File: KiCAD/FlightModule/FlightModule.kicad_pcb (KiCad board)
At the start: 2 copper layers, 90 x 70 mm, 19 parts, among them Q1 AO3400A, Q2 AO3400A, U1 ARDUINO_MKR_WAN_1310, U2 MCP2515-xST, U3 MCP2562-E-SN, U4 MB85RQ8MX, U5 MB85RQ8MX, U6 MB85RQ8MX

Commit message: 配線8割り終わり．次の作業....
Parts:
- removed IC1: ~, GPSShield:UBLOXLIB_SAM-M8Q
- removed U4, U6: MB85RQ8MX, Package_SO:SOIC-16W_7.5x10.3mm_P1.27mm
- added C10: 1u, Capacitor_SMD:C_0603_1608Metric_Pad1.08x0.95mm_HandSolder, F.Cu at (185.2, 104.9)
- added C11: 1u, Capacitor_SMD:C_0603_1608Metric_Pad1.08x0.95mm_HandSolder, F.Cu at (185.2, 98.6)
- added C13: 0.1uF, Capacitor_SMD:C_0603_1608Metric_Pad1.08x0.95mm_HandSolder, F.Cu at (160.5, 114.9)
- added C14: 0.1uF, Capacitor_SMD:C_0603_1608Metric_Pad1.08x0.95mm_HandSolder, B.Cu at (154.2, 105.5)
- added C15: 0.1uF, Capacitor_SMD:C_0603_1608Metric_Pad1.08x0.95mm_HandSolder, B.Cu at (122.7, 94.5)
- added C16: 1uF, Capacitor_SMD:C_1206_3216Metric_Pad1.33x1.80mm_HandSolder, F.Cu at (153.7, 68.1)
- added C17: 1uF, Capacitor_SMD:C_1206_3216Metric_Pad1.33x1.80mm_HandSolder, F.Cu at (166.1, 68.1)
- added C4: 0.1uF, Capacitor_SMD:C_0603_1608Metric_Pad1.08x0.95mm_HandSolder, F.Cu at (160.5, 120.1)
- added C5: 0.1uF, Capacitor_SMD:C_0603_1608Metric_Pad1.08x0.95mm_HandSolder, B.Cu at (170.9, 110.2)
- added C6: 15pF, Capacitor_SMD:C_0603_1608Metric_Pad1.08x0.95mm_HandSolder, B.Cu at (180.8, 94.1)
- added C7: 15pF, Capacitor_SMD:C_0603_1608Metric_Pad1.08x0.95mm_HandSolder, B.Cu at (164.3, 94.1)
- added C8: 0.1uF, Capacitor_SMD:C_0603_1608Metric_Pad1.08x0.95mm_HandSolder, B.Cu at (137.5, 120.8)
- added C9: 0.1uF, Capacitor_SMD:C_0603_1608Metric_Pad1.08x0.95mm_HandSolder, F.Cu at (135.6, 117.2)
- added D10: Green, LED_SMD:LED_0603_1608Metric_Pad1.05x0.95mm_HandSolder, F.Cu at (135.6, 67.0)
- added D11: GS1010FL, Diode_SMD:D_SOD-123F, F.Cu at (136.1, 75.4)
- added D12: Blue, LED_SMD:LED_0603_1608Metric_Pad1.05x0.95mm_HandSolder, F.Cu at (90.9, 82.5)
- added D7: Blue, LED_SMD:LED_0603_1608Metric_Pad1.05x0.95mm_HandSolder, F.Cu at (90.9, 80.0)
- added D8: Green, LED_SMD:LED_0603_1608Metric_Pad1.05x0.95mm_HandSolder, F.Cu at (144.1, 67.0)
- added D9: GS1010FL, Diode_SMD:D_SOD-123F, F.Cu at (142.1, 75.4)
- added J1: DF11B-8DP-2DS, TSRP_Connector_Hirose:DF11-8DP-2DS, F.Cu at (162.5, 128.0)
- added J4: DF51-2P-2DS, TSRP_Connector_Hirose:DF51-2P-2DS, F.Cu at (137.5, 134.8)
- added J5: DF51A-4P-2DSA, TSRP_Connector_Hirose:DF51A-4P-2DSA, F.Cu at (141.6, 68.4)
- added PS1: M78AR05-0.5, TSRP_IC:M78AR03305, F.Cu at (181.7, 113.9)
- added R11: 120R, Resistor_SMD:R_0603_1608Metric_Pad0.98x0.95mm_HandSolder, F.Cu at (164.6, 121.9)
- added R13: 680R, Resistor_SMD:R_0603_1608Metric_Pad0.98x0.95mm_HandSolder, F.Cu at (86.6, 84.7)
- added R14: 10kR, Resistor_SMD:R_0603_1608Metric_Pad0.98x0.95mm_HandSolder, B.Cu at (173.0, 110.2)
- added R15: 300, Resistor_SMD:R_0603_1608Metric_Pad0.98x0.95mm_HandSolder, F.Cu at (140.3, 82.9)
- added R16: 10k, Resistor_SMD:R_0603_1608Metric_Pad0.98x0.95mm_HandSolder, F.Cu at (140.3, 85.0)
- added R17: 2.4k, Resistor_SMD:R_0603_1608Metric_Pad0.98x0.95mm_HandSolder, F.Cu at (147.6, 67.0)
- added R18: 300, Resistor_SMD:R_0603_1608Metric_Pad0.98x0.95mm_HandSolder, F.Cu at (134.1, 82.9)
- added R19: 10k, Resistor_SMD:R_0603_1608Metric_Pad0.98x0.95mm_HandSolder, F.Cu at (134.1, 85.0)
- added R20: 2.4k, Resistor_SMD:R_0603_1608Metric_Pad0.98x0.95mm_HandSolder, F.Cu at (139.3, 67.0)
- added R21: 680R, Resistor_SMD:R_0603_1608Metric_Pad0.98x0.95mm_HandSolder, F.Cu at (86.6, 87.2)
- added R24: 10kR, Resistor_SMD:R_0603_1608Metric_Pad0.98x0.95mm_HandSolder, F.Cu at (135.6, 115.4)
- added R25: 10kR, Resistor_SMD:R_0603_1608Metric_Pad0.98x0.95mm_HandSolder, B.Cu at (139.4, 122.6)
- added R26: 4.7kR, Resistor_SMD:R_0603_1608Metric_Pad0.98x0.95mm_HandSolder, B.Cu at (136.5, 105.4)
- added R27: 100k, Resistor_SMD:R_0603_1608Metric_Pad0.98x0.95mm_HandSolder, F.Cu at (169.9, 85.1)
- added R28: 0, Resistor_SMD:R_0603_1608Metric_Pad0.98x0.95mm_HandSolder, F.Cu at (160.8, 67.6)
- added R29: 4.7k, Resistor_SMD:R_0603_1608Metric_Pad0.98x0.95mm_HandSolder, F.Cu at (148.1, 84.8)
- added R30: 4.7k, Resistor_SMD:R_0603_1608Metric_Pad0.98x0.95mm_HandSolder, F.Cu at (149.6, 79.5)
- added U7: TC7S14F, Package_TO_SOT_SMD:TSOT-23-5_HandSoldering, F.Cu at (134.7, 120.3)
- added U8: MCP2562-E-SN, Package_SO:SOIC-8_3.9x4.9mm_P1.27mm, F.Cu at (164.6, 117.1)
- added U9: MCP2515-xST, Package_SO:TSSOP-20_4.4x6.5mm_P0.65mm, B.Cu at (170.7, 103.3)
- added Ux1: ARDUINO_MKR_WAN_1310, TSRP_Arduino:BOARD_ARDUINO_MKR_WAN_1310, F.Cu at (143.0, 100.0)
- added Y1: 8MHz, Crystal:Crystal_SMD_HC49-SD, B.Cu at (172.6, 95.1)
- D1, D3: value G -> Blue
- D2: value GS1010FL -> Blue; footprint Diode_SMD:D_SOD-123F -> LED_SMD:LED_0603_1608Metric_Pad1.05x0.95mm_HandSolder
- D4: value GS1010FL -> R; footprint Diode_SMD:D_SOD-123F -> LED_SMD:LED_0603_1608Metric_Pad1.05x0.95mm_HandSolder
- R1: value 300R -> 4.7kR; moved to B.Cu
- R2: value 10kR -> 4.7kR; moved to B.Cu
- R3: value 2.4kR -> 680R
- R4: value 300R -> 680R
- R5: value 10kR -> 680R
- U1: value ARDUINO_MKR_WAN_1310 -> MB85RQ8MX; footprint ARDUINO_MKR_WAN_1310:BOARD_ARDUINO_MKR_WAN_1310 -> Package_SO:SOIC-16W_7.5x10.3mm_P1.27mm; moved to B.Cu
- U2: value MCP2515-xST -> MB85RQ8MX; footprint Package_SO:TSSOP-20_4.4x6.5mm_P0.65mm -> Package_SO:SOIC-16W_7.5x10.3mm_P1.27mm; moved to B.Cu
- U3: value MCP2562-E-SN -> SAM-M8Q-0-10; footprint Package_SO:SOIC-8_3.9x4.9mm_P1.27mm -> TSRP_IC:MODULE_SAM-M8Q-0-10
- U5: value MB85RQ8MX -> NCV8114BSN330T1G; footprint Package_SO:SOIC-16W_7.5x10.3mm_P1.27mm -> Package_TO_SOT_SMD:TSOT-23-5
- moved D3 140.2 mm to (90.9, 77.2)
- moved R3 130.6 mm to (86.6, 77.2)
- moved R5 130.6 mm to (86.6, 82.2)
- moved R4 130.6 mm to (86.6, 79.7)
- moved D1 122.6 mm to (90.9, 72.2)
- moved D2 117.8 mm to (90.9, 74.8)
- moved Q2 107.2 mm to (134.1, 79.4), turned to 90 degrees
- moved U2 91.2 mm to (130.0, 100.0), turned to 90 degrees
- moved Q1 89.0 mm to (140.3, 79.4), turned to 90 degrees
- moved R1 72.7 mm to (140.0, 94.5), turned to 90 degrees
- moved U3 60.7 mm to (160.0, 78.0), turned to -90 degrees
- moved R2 56.4 mm to (157.2, 98.4), turned to -90 degrees
- moved R6 48.7 mm to (170.7, 132.3), turned to -90 degrees
- moved U5 43.4 mm to (187.2, 101.7), turned to 90 degrees
- moved D4 23.1 mm to (168.8, 132.3), turned to 90 degrees
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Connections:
- D1 pad 1: Net-(D1-K) -> GND
- D2 pad 1: +12V -> GND
- D2 pad 2: Net-(D1-K) -> Net-(D2-A)
- D3 pad 1: Net-(D3-K) -> GND
- D4 pad 1: +12V -> GND
- D4 pad 2: Net-(D3-K) -> Net-(D4-A)
- Q1 pad 3: Net-(D1-K) -> Net-(D8-K)
- Q2 pad 3: Net-(D3-K) -> Net-(D10-K)
- R1 pad 1: unconnected-(R1-Pad1) -> +3.3V
- R1 pad 2: Net-(Q1-G) -> SPI_~{CS}_FeRAM0
- R2 pad 1: GND -> +3.3V
- R2 pad 2: Net-(Q1-G) -> SPI_CS_MCP2515
- R3 pad 1: +12V -> LORA_RECEIVE_STATUS
- R4 pad 1: unconnected-(R4-Pad1) -> LORA_SEND_STATUS
- R4 pad 2: Net-(Q2-G) -> Net-(D2-A)
- R5 pad 1: GND -> GNSS_STATUS
- R5 pad 2: Net-(Q2-G) -> Net-(D3-A)
- R6 pad 2: Net-(D3-A) -> Net-(D4-A)
- U2 pad 1: unconnected-(U2-TXCAN-Pad1) -> +3.3V
- U2 pad 10: unconnected-(U2-VSS-Pad10) -> GND
- U2 pad 15: unconnected-(U2-NC-Pad15) -> SPI_MOSI
- U2 pad 16: unconnected-(U2-SI-Pad16) -> SPI_SCLK
- U2 pad 2: unconnected-(U2-RXCAN-Pad2) -> +3.3V
- U2 pad 7: unconnected-(U2-~{TX2RTS}-Pad7) -> SPI_~{CS}_FeRAM1
- U2 pad 8: unconnected-(U2-OSC2-Pad8) -> SPI_MISO
- U2 pad 9: unconnected-(U2-OSC1-Pad9) -> +3.3V
- U3 pad 1: unconnected-(U3-TXD-Pad1) -> GND
- U3 pad 2: unconnected-(U3-VSS-Pad2) -> +3.3V
- U3 pad 3: unconnected-(U3-VDD-Pad3) -> Net-(U3-V_BCKP)
- U3 pad 4: unconnected-(U3-RXD-Pad4) -> GND
- U3 pad 5: unconnected-(U3-Vio-Pad5) -> GND
- U3 pad 6: unconnected-(U3-CANL-Pad6) -> GND
- U5 pad 1: unconnected-(U5-nHOLD-Pad1) -> +5V
- U5 pad 2: unconnected-(U5-VDD-Pad2) -> GND
- U5 pad 3: (no net) -> +5V
- U5 pad 4: (no net) -> unconnected-(U5-NC-Pad4)
- U5 pad 5: (no net) -> +3.3V
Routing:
- net +3.3V: track 0.00 -> 264.6 mm, vias 0 -> 5
- net +12V: track 0.00 -> 174.2 mm, vias 0 -> 3
- net +5V: track 0.00 -> 106.6 mm, vias 0 -> 2
- net SPI_MOSI: track 0.00 -> 71.4 mm, vias 0 -> 6
- net SPI_MISO: track 0.00 -> 70.9 mm, vias 0 -> 4
- net SPI_SCLK: track 0.00 -> 65.7 mm, vias 0 -> 5
- net SPI_CS_MCP2515: track 0.00 -> 30.2 mm, vias 0 -> 2
- net FLIGHT_PIN: track 0.00 -> 29.0 mm, vias 0 -> 1
- net SPI_~{CS}_FeRAM0: track 0.00 -> 26.5 mm, vias 0 -> 2
- net CAN_RX: track 0.00 -> 21.5 mm, vias 0 -> 1
- net CAN_TX: track 0.00 -> 21.4 mm, vias 0 -> 1
- net I2C_SCL: track 0.00 -> 17.4 mm
- net Net-(J4-Pin_2): track 0.00 -> 17.2 mm, vias 0 -> 1
- net SPI_~{CS}_FeRAM1: track 0.00 -> 15.8 mm
- net Net-(D10-K): track 0.00 -> 14.9 mm
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- added copper zone on F.Cu, net +3.3V
- added copper zone on F.Cu, net +5V
- added copper zone on B.Cu, net GND
- added copper zone on F.Cu, net GND

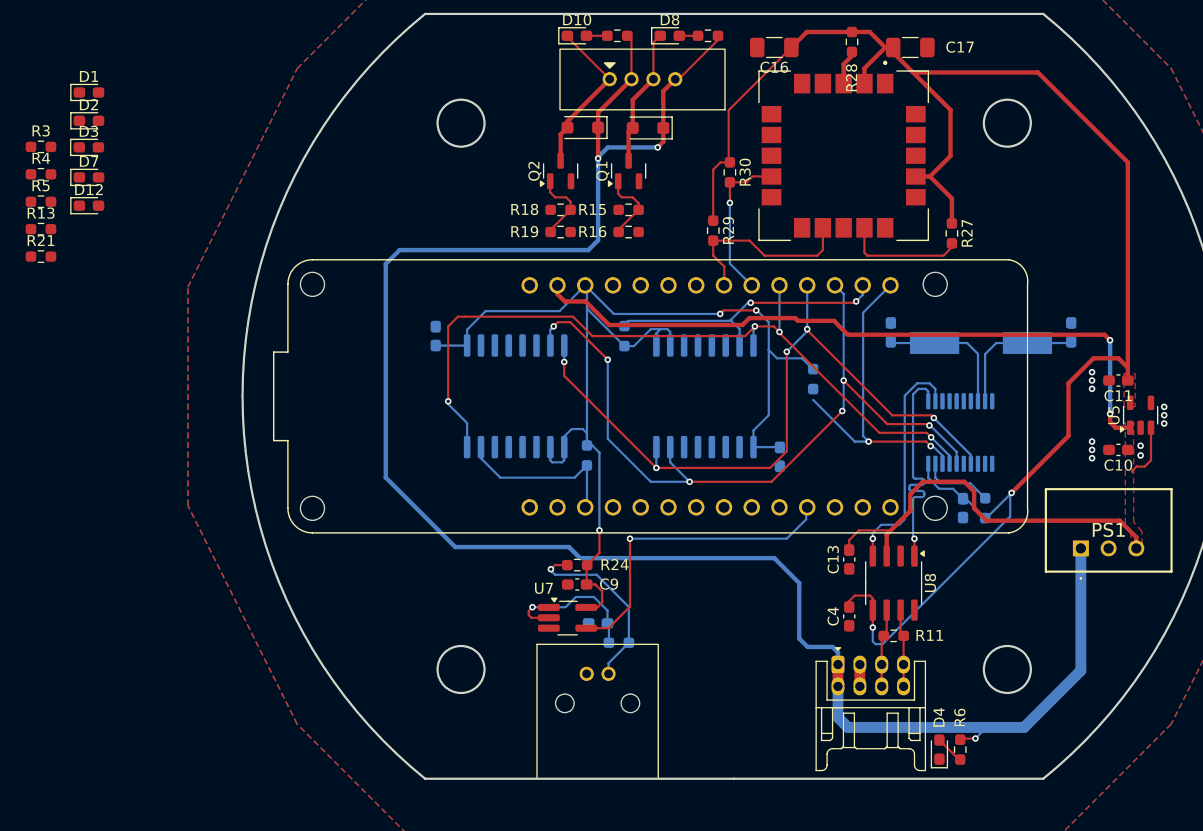
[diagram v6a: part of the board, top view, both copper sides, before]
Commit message: ステータスLEDの表示まで完了
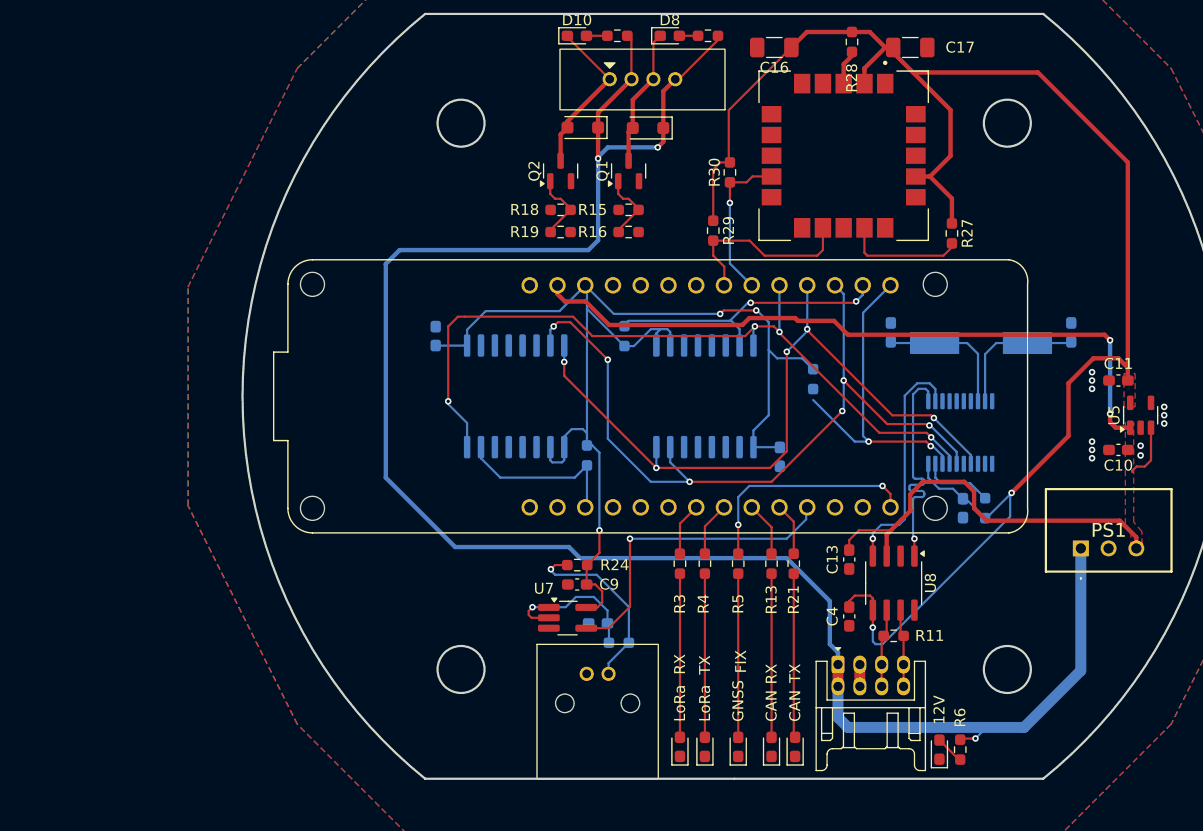
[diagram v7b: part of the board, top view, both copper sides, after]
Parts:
- moved D12 81.4 mm to (155.6, 132.1), turned to 90 degrees
- moved D7 81.4 mm to (153.4, 132.1), turned to 90 degrees
- moved D3 80.9 mm to (150.4, 132.1), turned to 90 degrees
- moved D1 80.7 mm to (145.0, 132.1), turned to 90 degrees
- moved D2 80.4 mm to (147.3, 132.1), turned to 90 degrees
- moved R21 74.4 mm to (155.4, 115.3), turned to -90 degrees
- moved R13 73.5 mm to (153.4, 115.3), turned to -90 degrees
- moved R5 71.9 mm to (150.4, 115.3), turned to -90 degrees
- moved R4 70.4 mm to (147.3, 115.3), turned to -90 degrees
- moved R3 69.8 mm to (145.0, 115.3), turned to -90 degrees
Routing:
- net GNSS_STATUS: track 0.00 -> 21.1 mm, vias 0 -> 2
- net Net-(D12-A): track 0.00 -> 15.0 mm
- net Net-(D7-A): track 0.00 -> 15.0 mm
- net Net-(D3-A): track 0.00 -> 15.0 mm
- net Net-(D2-A): track 0.00 -> 15.0 mm
- net Net-(D1-A): track 0.00 -> 15.0 mm
- net CAN_RECEIVE_STATUS: track 0.00 -> 4.99 mm
- net LORA_SEND_STATUS: track 0.00 -> 4.97 mm
- net LORA_RECEIVE_STATUS: track 0.00 -> 4.86 mm
- net CAN_SEND_STATUS: track 0.00 -> 4.78 mm
- net +12V: track 174.2 -> 173.6 mm
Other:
- board text added: "12V"
- board text added: "CAN"
- board text added: "FIX"
- board text added: "GNSS"
- board text added: "LoRa"
- board text added: "RX"
- board text added: "TX"

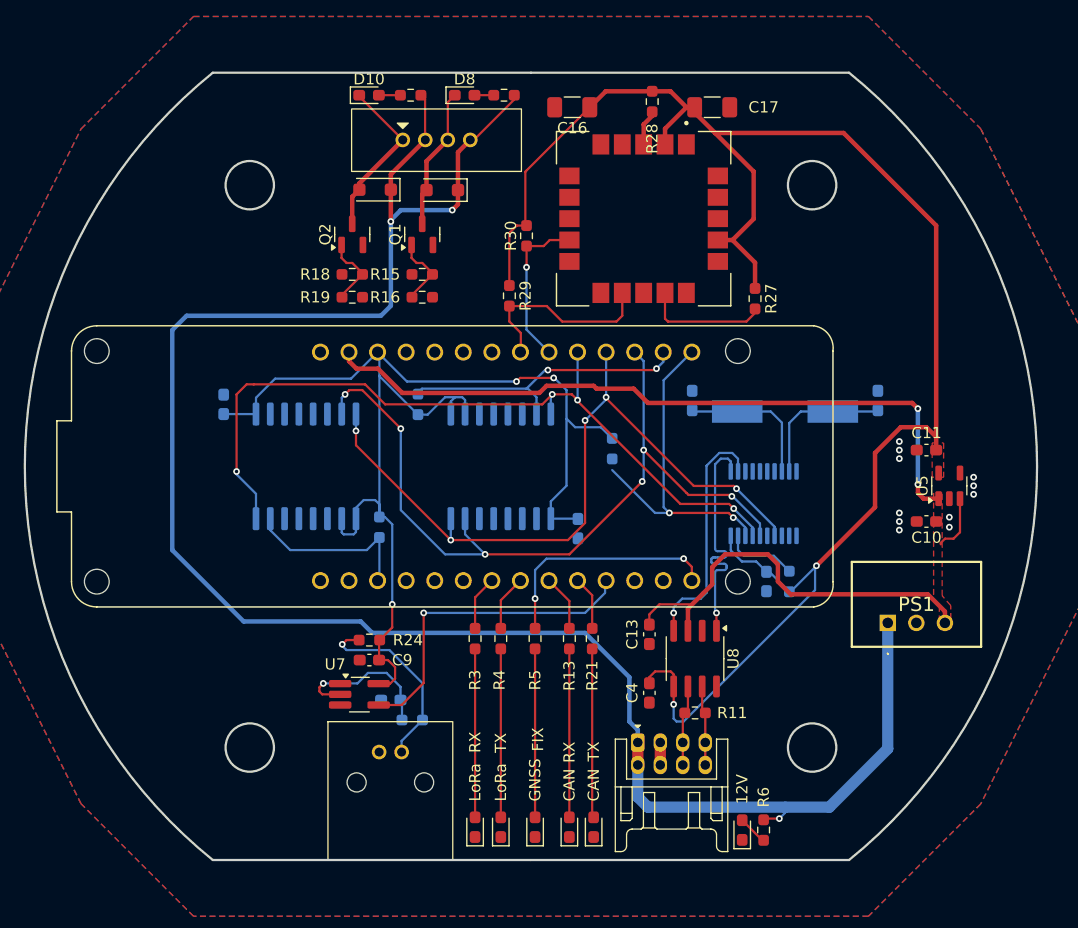
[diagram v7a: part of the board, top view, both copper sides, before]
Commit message: FeRAMを3個に増設
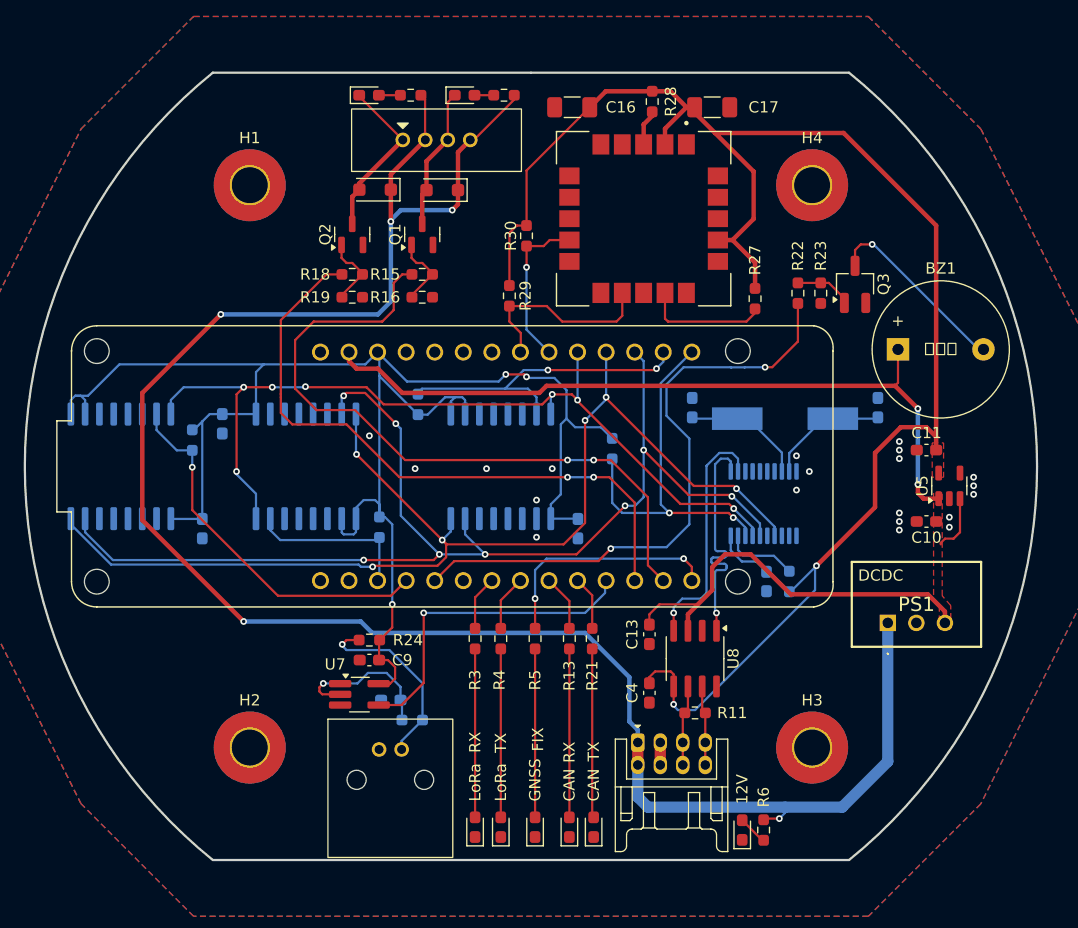
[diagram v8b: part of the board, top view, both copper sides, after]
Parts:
- added BZ1: UGCM1205XP, Buzzer_Beeper:Buzzer_12x9.5RM7.6, F.Cu at (182.6, 89.6)
- added C18: 0.1uF, Capacitor_SMD:C_0603_1608Metric_Pad1.08x0.95mm_HandSolder, B.Cu at (120.8, 105.5)
- added H1: MountingHole_Pad, MountingHole:MountingHole_3.2mm_M3_Pad_TopBottom, F.Cu at (125.0, 75.0)
- added H2: MountingHole_Pad, MountingHole:MountingHole_3.2mm_M3_Pad_TopBottom, F.Cu at (125.0, 125.0)
- added H3: MountingHole_Pad, MountingHole:MountingHole_3.2mm_M3_Pad_TopBottom, F.Cu at (175.0, 125.0)
- added H4: MountingHole_Pad, MountingHole:MountingHole_3.2mm_M3_Pad_TopBottom, F.Cu at (175.0, 75.0)
- added Q3: 2SC3325-Y, Package_TO_SOT_SMD:SC-59_Handsoldering, F.Cu at (178.8, 83.8)
- added R22: 4.7kR, Resistor_SMD:R_0603_1608Metric_Pad0.98x0.95mm_HandSolder, F.Cu at (173.7, 84.6)
- added R23: 10kR, Resistor_SMD:R_0603_1608Metric_Pad0.98x0.95mm_HandSolder, F.Cu at (175.8, 84.6)
- added R31: 4.7kR, Resistor_SMD:R_0603_1608Metric_Pad0.98x0.95mm_HandSolder, B.Cu at (119.9, 97.7)
- added U4: MB85RQ8MX, Package_SO:SOIC-16W_7.5x10.3mm_P1.27mm, B.Cu at (113.5, 100.0)
- moved C15 1.73 mm to (122.6, 96.2), turned to -90 degrees
- moved C6 0.64 mm to (180.8, 94.8)
- moved C7 0.64 mm to (164.3, 94.8)
- moved Y1 0.63 mm to (172.6, 95.8)
- moved J4 0.23 mm to (137.5, 134.6)
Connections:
- Ux1 pad J3_4: unconnected-(Ux1-PB03/D17/AIN(11)/A2-PadJ3_4) -> SPI_~{CS}_FeRAM2
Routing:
- net SN3: track 0.00 -> 61.9 mm, vias 0 -> 2
- net SN4: track 0.00 -> 57.1 mm, vias 0 -> 2
- net BUZZER: track 0.00 -> 54.7 mm, vias 0 -> 2
- net SPI_SCLK: track 65.7 -> 104.3 mm, vias 5 -> 6
- net +3.3V: track 264.6 -> 300.8 mm
- net SPI_MOSI: track 71.4 -> 106.3 mm, vias 6 -> 8
- net SPI_~{CS}_FeRAM2: track 0.00 -> 33.4 mm, vias 0 -> 1
- net Net-(BZ1-+): track 0.00 -> 16.5 mm, vias 0 -> 1
- net SPI_MISO: track 70.9 -> 78.9 mm, vias 4 -> 7
- net Net-(Q3-B): track 0.00 -> 5.10 mm
- net SPI_CS_MCP2515: track 30.2 -> 33.2 mm
- net SPI_~{CS}_FeRAM0: track 26.5 -> 28.4 mm
- net OSC2: track 12.8 -> 10.9 mm
- net OSC1: track 12.7 -> 10.8 mm
- net +5V: track 106.6 -> 108.2 mm
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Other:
- outline, holes or cut-outs redrawn
- board text added: "DCDC"
- board text added: "ぶざー"
